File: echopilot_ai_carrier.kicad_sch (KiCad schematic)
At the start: 10 parts, among them J1 Conn_01x01, J2 Conn_01x01, J3 Conn_01x01, J4 Conn_01x01

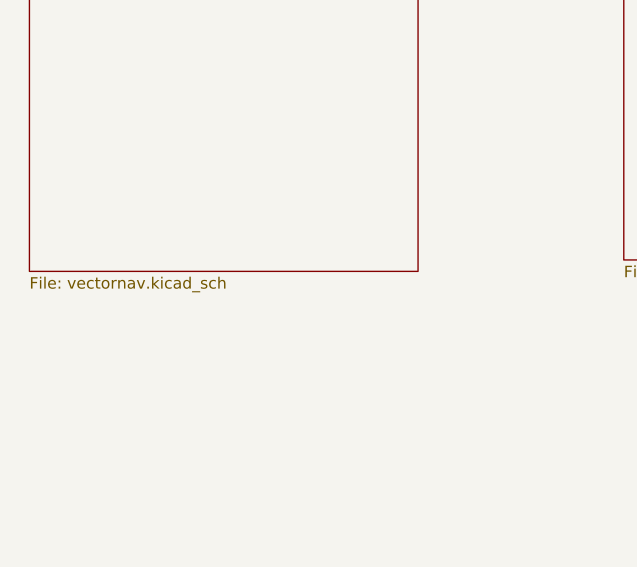
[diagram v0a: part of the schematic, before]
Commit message: change vectornav schematic naming for clarity
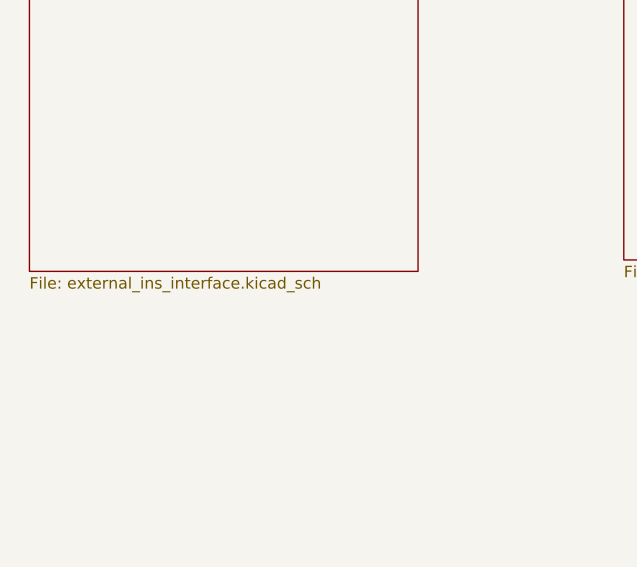
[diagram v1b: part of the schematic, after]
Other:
- sheet External INS: file vectornav.kicad_sch -> external_ins_interface.kicad_sch
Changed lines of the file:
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@@
     (pin "1")
     (instances
-      (project "pixc4-jetson-universal-carrier"
+      (project "echopilot_ai_carrier"
         (path "/c1cd829b-ce6d-45d4-ac65-d2dab15a61f6"
           (reference "J1") (unit 1)
@@
     (pin "1")
     (instances
-      (project "pixc4-jetson-universal-carrier"
+      (project "echopilot_ai_carrier"
         (path "/c1cd829b-ce6d-45d4-ac65-d2dab15a61f6"
           (reference "#PWR01") (unit 1)
@@
     (pin "1")
     (instances
-      (project "pixc4-jetson-universal-carrier"
+      (project "echopilot_ai_carrier"
         (path "/c1cd829b-ce6d-45d4-ac65-d2dab15a61f6"
           (reference "J2") (unit 1)
@@
     (pin "1")
     (instances
-      (project "pixc4-jetson-universal-carrier"
+      (project "echopilot_ai_carrier"
         (path "/c1cd829b-ce6d-45d4-ac65-d2dab15a61f6"
           (reference "#PWR02") (unit 1)
@@
     (pin "1")
     (instances
-      (project "pixc4-jetson-universal-carrier"
+      (project "echopilot_ai_carrier"
         (path "/c1cd829b-ce6d-45d4-ac65-d2dab15a61f6"
           (reference "J3") (unit 1)
@@
     (pin "1")
     (instances
-      (project "pixc4-jetson-universal-carrier"
+      (project "echopilot_ai_carrier"
         (path "/c1cd829b-ce6d-45d4-ac65-d2dab15a61f6"
           (reference "#PWR03") (unit 1)
@@
     (pin "1")
     (instances
-      (project "pixc4-jetson-universal-carrier"
+      (project "echopilot_ai_carrier"
         (path "/c1cd829b-ce6d-45d4-ac65-d2dab15a61f6"
           (reference "J4") (unit 1)
@@
     (pin "1")
     (instances
-      (project "pixc4-jetson-universal-carrier"
+      (project "echopilot_ai_carrier"
         (path "/c1cd829b-ce6d-45d4-ac65-d2dab15a61f6"
           (reference "#PWR04") (unit 1)
@@
     )
     (instances
-      (project "pixc4-jetson-universal-carrier"
+      (project "echopilot_ai_carrier"
         (path "/c1cd829b-ce6d-45d4-ac65-d2dab15a61f6"
           (reference "FID2") (unit 1)
@@
     )
     (instances
-      (project "pixc4-jetson-universal-carrier"
+      (project "echopilot_ai_carrier"
         (path "/c1cd829b-ce6d-45d4-ac65-d2dab15a61f6"
           (reference "FID4") (unit 1)
@@
     )
     (instances
-      (project "pixc4-jetson-universal-carrier"
+      (project "echopilot_ai_carrier"
         (path "/c1cd829b-ce6d-45d4-ac65-d2dab15a61f6"
           (reference "FID5") (unit 1)
@@
     )
     (instances
-      (project "pixc4-jetson-universal-carrier"
+      (project "echopilot_ai_carrier"
         (path "/c1cd829b-ce6d-45d4-ac65-d2dab15a61f6"
           (reference "FID1") (unit 1)
@@
     )
     (instances
-      (project "pixc4-jetson-universal-carrier"
+      (project "echopilot_ai_carrier"
         (path "/c1cd829b-ce6d-45d4-ac65-d2dab15a61f6"
           (reference "FID3") (unit 1)
@@
     )
     (instances
-      (project "pixc4-jetson-universal-carrier"
+      (project "echopilot_ai_carrier"
         (path "/c1cd829b-ce6d-45d4-ac65-d2dab15a61f6"
           (reference "FID6") (unit 1)
@@
     )
     (instances
-      (project "pixc4-jetson-universal-carrier"
+      (project "echopilot_ai_carrier"
         (path "/c1cd829b-ce6d-45d4-ac65-d2dab15a61f6" (page "4"))
       )
@@
     )
     (instances
-      (project "pixc4-jetson-universal-carrier"
+      (project "echopilot_ai_carrier"
         (path "/c1cd829b-ce6d-45d4-ac65-d2dab15a61f6" (page "2"))
       )
@@
     )
     (instances
-      (project "pixc4-jetson-universal-carrier"
+      (project "echopilot_ai_carrier"
         (path "/c1cd829b-ce6d-45d4-ac65-d2dab15a61f6" (page "3"))
       )
@@
       (effects (font (size 1.27 1.27)) (justify left bottom))
     )
-    (property "Sheetfile" "vectornav.kicad_sch" (at 51.435 206.9596 0)
-      (effects (font (size 1.27 1.27)) (justify left top))
-    )
-    (instances
-      (project "pixc4-jetson-universal-carrier"
+    (property "Sheetfile" "external_ins_interface.kicad_sch" (at 51.435 206.9596 0)
+      (effects (font (size 1.27 1.27)) (justify left top))
+    )
+    (instances
+      (project "echopilot_ai_carrier"
         (path "/c1cd829b-ce6d-45d4-ac65-d2dab15a61f6" (page "5"))
       )
@@
     )
     (instances
-      (project "pixc4-jetson-universal-carrier"
+      (project "echopilot_ai_carrier"
         (path "/c1cd829b-ce6d-45d4-ac65-d2dab15a61f6" (page "6"))
       )
@@
     )
     (instances
-      (project "pixc4-jetson-universal-carrier"
+      (project "echopilot_ai_carrier"
         (path "/c1cd829b-ce6d-45d4-ac65-d2dab15a61f6" (page "7"))
       )

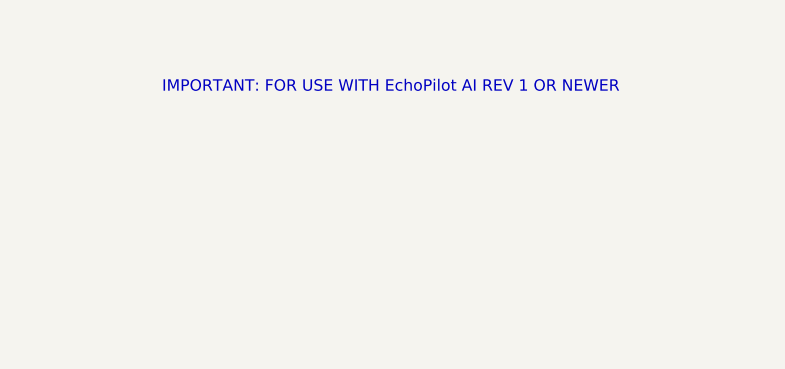
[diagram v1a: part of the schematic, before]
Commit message: updates for Rev1B boards, pinout changes on J5 and J8
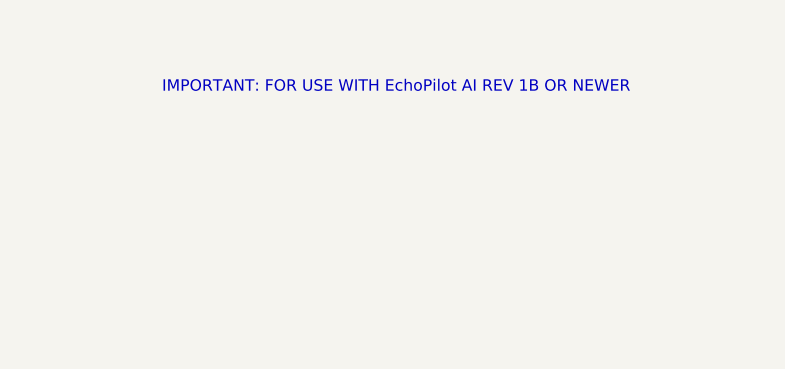
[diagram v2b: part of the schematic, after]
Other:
- note added: "IMPORTANT: FOR USE WITH EchoPilot AI REV 1B OR NEWER"
- note removed: "IMPORTANT: FOR USE WITH EchoPilot AI REV 1 OR NEWER"
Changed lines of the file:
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@@
     )
   )
-  (text "IMPORTANT: FOR USE WITH EchoPilot AI REV 1 OR NEWER"
+  (text "IMPORTANT: FOR USE WITH EchoPilot AI REV 1B OR NEWER"
     (at 187.96 43.815 0)
     (effects (font (size 1.27 1.27)) (justify left bottom))
